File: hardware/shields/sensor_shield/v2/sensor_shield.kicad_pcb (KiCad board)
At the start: 2 copper layers, 34 x 33.8 mm, 4 parts

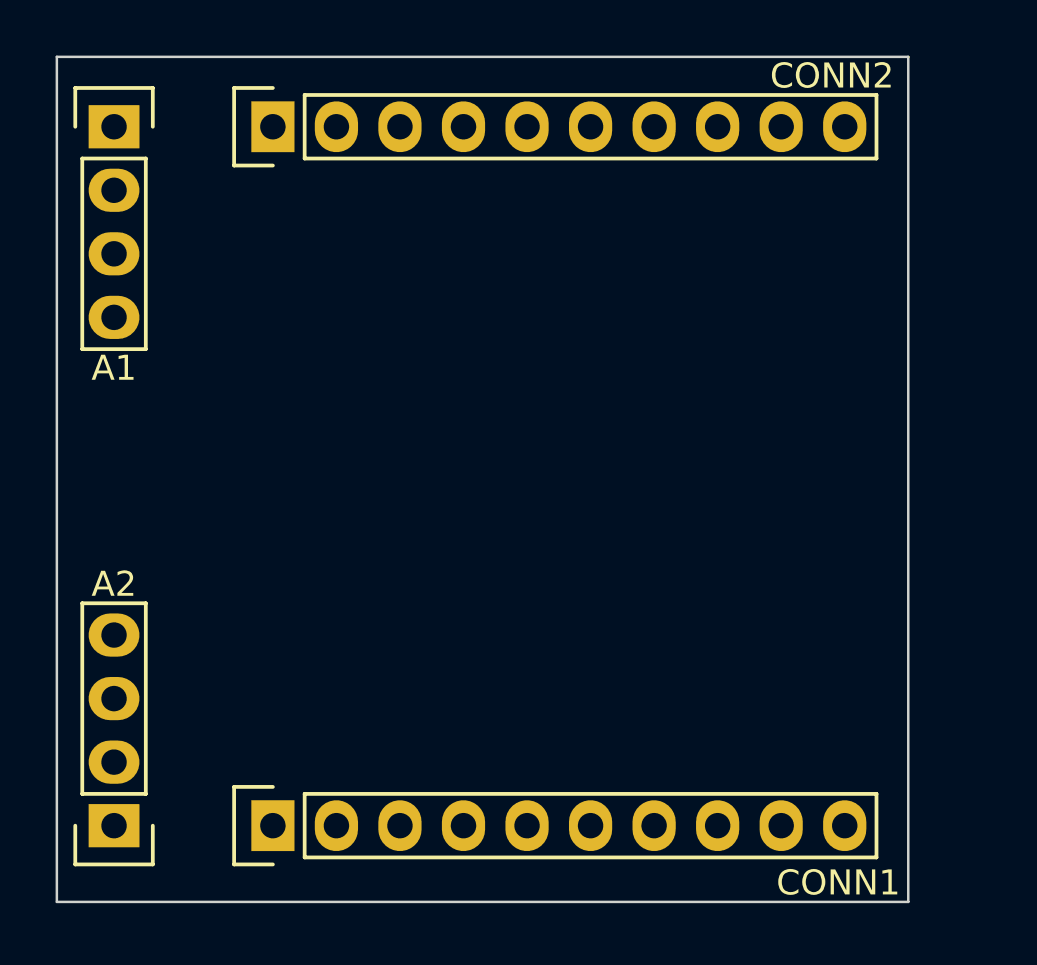
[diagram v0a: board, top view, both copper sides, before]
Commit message: Adding some footprints
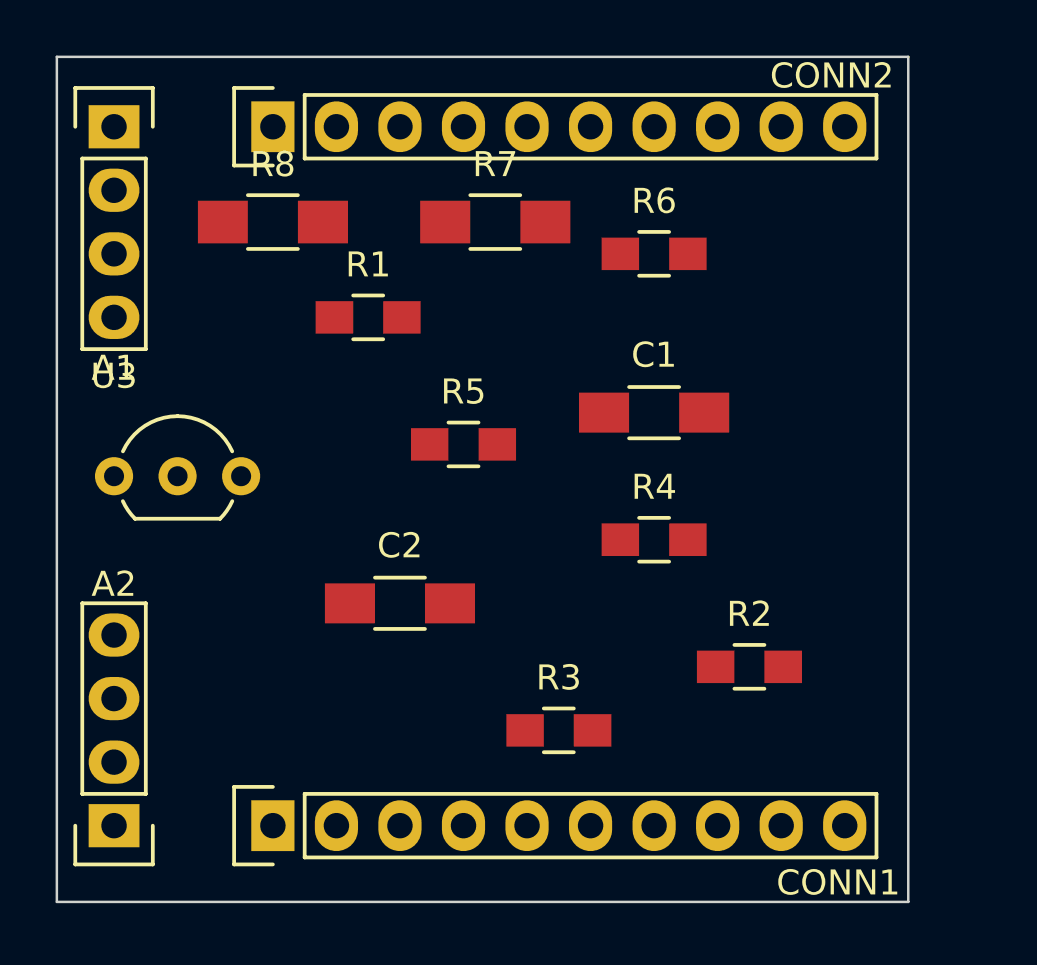
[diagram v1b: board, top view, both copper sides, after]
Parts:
- added C1: 100n, Capacitors_SMD:C_1206_HandSoldering, F.Cu at (62.2, 39.4)
- added C2: 100n, Capacitors_SMD:C_1206_HandSoldering, F.Cu at (52.1, 47.0)
- added R1: 1.8k, Resistors_SMD:R_0805_HandSoldering, F.Cu at (50.8, 35.6)
- added R2: 1.8k, Resistors_SMD:R_0805_HandSoldering, F.Cu at (66.0, 49.5)
- added R3: 100k, Resistors_SMD:R_0805_HandSoldering, F.Cu at (58.4, 52.1)
- added R4: 4.7k, Resistors_SMD:R_0805_HandSoldering, F.Cu at (62.2, 44.5)
- added R5: 200k, Resistors_SMD:R_0805_HandSoldering, F.Cu at (54.6, 40.6)
- added R6: 200k, Resistors_SMD:R_0805_HandSoldering, F.Cu at (62.2, 33.0)
- added R7: 0, Resistors_SMD:R_1206_HandSoldering, F.Cu at (55.9, 31.8)
- added R8: 0, Resistors_SMD:R_1206_HandSoldering, F.Cu at (47.0, 31.8)
- added U3: DS18x20, TO_SOT_Packages_THT:TO-92_Inline_Wide, F.Cu at (40.6, 41.9)

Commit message: Routing of sensor shield complete
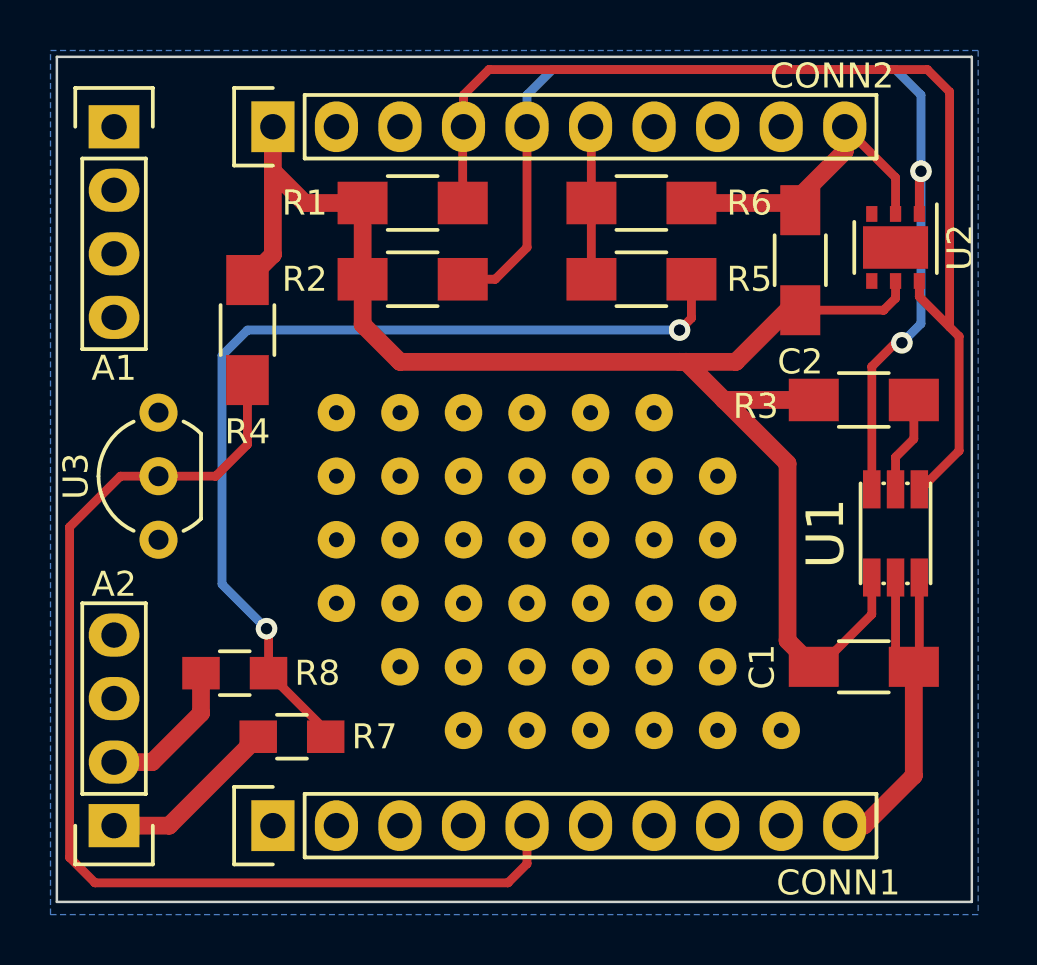
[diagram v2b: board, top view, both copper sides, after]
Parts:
- added ?: , pcb_helpers:pad, F.Cu at (49.5, 39.4)
- added ?: , pcb_helpers:pad, F.Cu at (57.1, 41.9)
- added ?: , pcb_helpers:pad, F.Cu at (59.7, 41.9)
- added ?: , pcb_helpers:pad, F.Cu at (62.2, 41.9)
- added ?: , pcb_helpers:pad, F.Cu at (64.8, 41.9)
- added ?: , pcb_helpers:pad, F.Cu at (49.5, 44.5)
- added ?: , pcb_helpers:pad, F.Cu at (52.1, 44.5)
- added ?: , pcb_helpers:pad, F.Cu at (54.6, 44.5)
- added ?: , pcb_helpers:pad, F.Cu at (57.1, 44.5)
- added ?: , pcb_helpers:pad, F.Cu at (59.7, 44.5)
- added ?: , pcb_helpers:pad, F.Cu at (62.2, 44.5)
- added ?: , pcb_helpers:pad, F.Cu at (52.1, 39.4)
- added ?: , pcb_helpers:pad, F.Cu at (64.8, 44.5)
- added ?: , pcb_helpers:pad, F.Cu at (49.5, 47.0)
- added ?: , pcb_helpers:pad, F.Cu at (52.1, 47.0)
- added ?: , pcb_helpers:pad, F.Cu at (54.6, 47.0)
- added ?: , pcb_helpers:pad, F.Cu at (57.1, 47.0)
- added ?: , pcb_helpers:pad, F.Cu at (59.7, 47.0)
- added ?: , pcb_helpers:pad, F.Cu at (62.2, 47.0)
- added ?: , pcb_helpers:pad, F.Cu at (64.8, 47.0)
- added ?: , pcb_helpers:pad, F.Cu at (52.1, 49.5)
- added ?: , pcb_helpers:pad, F.Cu at (54.6, 49.5)
- added ?: , pcb_helpers:pad, F.Cu at (54.6, 39.4)
- added ?: , pcb_helpers:pad, F.Cu at (57.1, 49.5)
- added ?: , pcb_helpers:pad, F.Cu at (59.7, 49.5)
- added ?: , pcb_helpers:pad, F.Cu at (62.2, 49.5)
- added ?: , pcb_helpers:pad, F.Cu at (64.8, 49.5)
- added ?: , pcb_helpers:pad, F.Cu at (64.8, 52.1)
- added ?: , pcb_helpers:pad, F.Cu at (62.2, 52.1)
- added ?: , pcb_helpers:pad, F.Cu at (59.7, 52.1)
- added ?: , pcb_helpers:pad, F.Cu at (57.1, 52.1)
- added ?: , pcb_helpers:pad, F.Cu at (54.6, 52.1)
- added ?: , pcb_helpers:pad, F.Cu at (67.3, 52.1)
- added ?: , pcb_helpers:pad, F.Cu at (57.1, 39.4)
- added ?: , pcb_helpers:pad, F.Cu at (59.7, 39.4)
- added ?: , pcb_helpers:pad, F.Cu at (62.2, 39.4)
- added ?: , pcb_helpers:pad, F.Cu at (49.5, 41.9)
- added ?: , pcb_helpers:pad, F.Cu at (52.1, 41.9)
- added ?: , pcb_helpers:pad, F.Cu at (54.6, 41.9)
- added U1: TSL2561, BugOne:TMB6, F.Cu at (71.9, 44.2)
- added U2: HTU2XD, Housings_DFN_QFN:DFN-6-1EP_3x3mm_Pitch0.95mm, F.Cu at (71.9, 32.8)
- R1, R2, R3, R4, R5, R6: footprint Resistors_SMD:R_0805_HandSoldering -> Resistors_SMD:R_1206_HandSoldering
- R7, R8: footprint Resistors_SMD:R_1206_HandSoldering -> Resistors_SMD:R_0805_HandSoldering
- moved R7 22.1 mm to (47.8, 52.3)
- moved C2 21.1 mm to (68.1, 33.3), turned to 90 degrees
- moved R2 20.5 mm to (52.6, 34.0)
- moved R4 18.3 mm to (46.0, 36.1), turned to 270 degrees
- moved R8 18.1 mm to (45.5, 49.8)
- moved R3 18.0 mm to (70.6, 38.9)
- moved C1 13.2 mm to (70.6, 49.5)
- moved R5 9.71 mm to (61.7, 34.0), turned to 180 degrees
- moved R1 4.91 mm to (52.6, 31.0)
- moved U3 3.10 mm to (42.4, 44.5), turned to 90 degrees
- moved R6 2.09 mm to (61.7, 31.0)
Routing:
- net VEE: track 0.00 -> 62.0 mm
- net PB1: track 0.00 -> 44.8 mm
- net SDA: track 0.00 -> 44.8 mm, vias 0 -> 2
- net SCL: track 0.00 -> 43.6 mm
- net Net-(R5-Pad1): track 0.00 -> 37.9 mm, vias 0 -> 2
- net GND: track 0.00 -> 27.8 mm
- net VSS: track 0.00 -> 7.23 mm
- net PC3: track 0.00 -> 6.11 mm
- net VCC: track 0.00 -> 5.89 mm
- net Net-(R3-Pad2): track 0.00 -> 3.87 mm
- added copper zone on B.Cu, net GND
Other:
- board size 34 x 33.8 mm -> 36.6 x 33.8 mm
- net class Default: clearance 0.254 -> 0.1524
- net class Power: clearance 0.254 -> 0.1524
- net class Signal: clearance 0.254 -> 0.1524
- rule trace_clearance: 0.254 -> 0.1524
- board text added: "U1"

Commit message: Minor fixes
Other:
- board text removed: "U1"

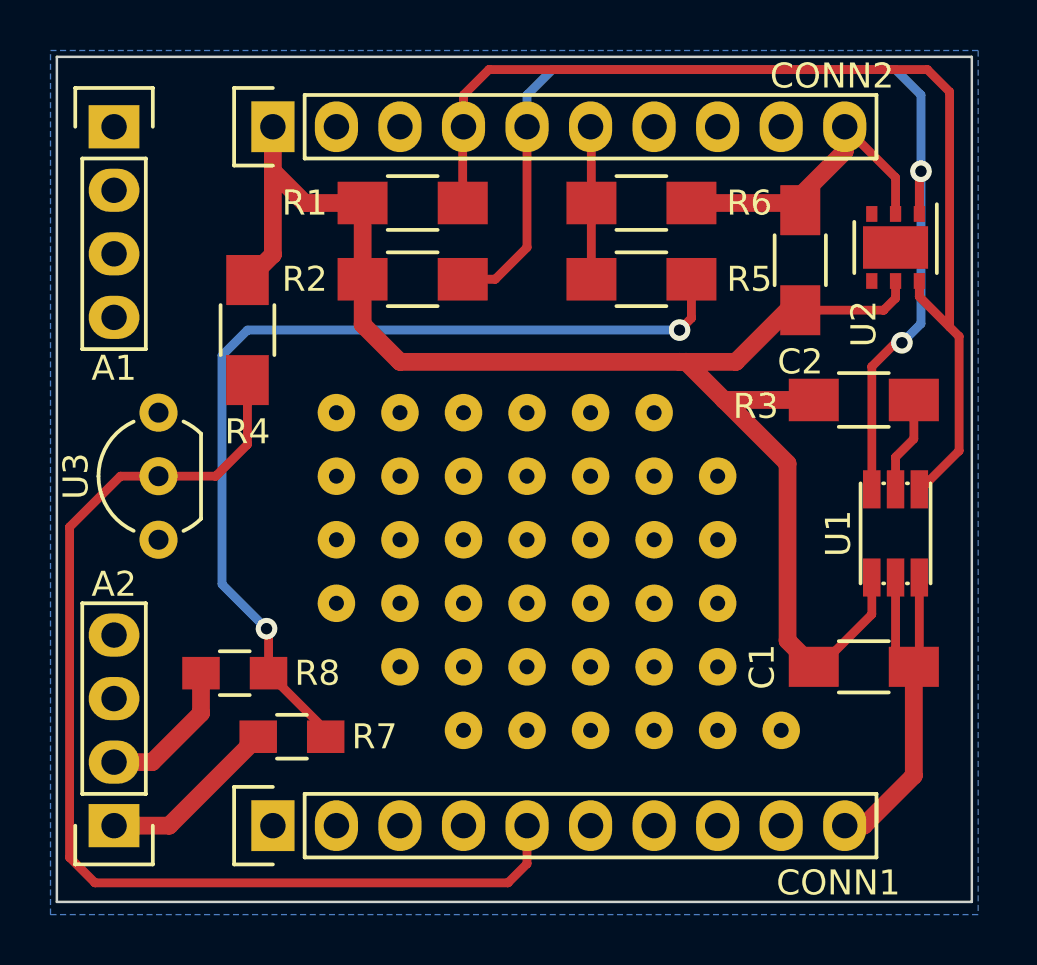
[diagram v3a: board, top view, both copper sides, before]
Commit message: Minor fixes on sensor shield
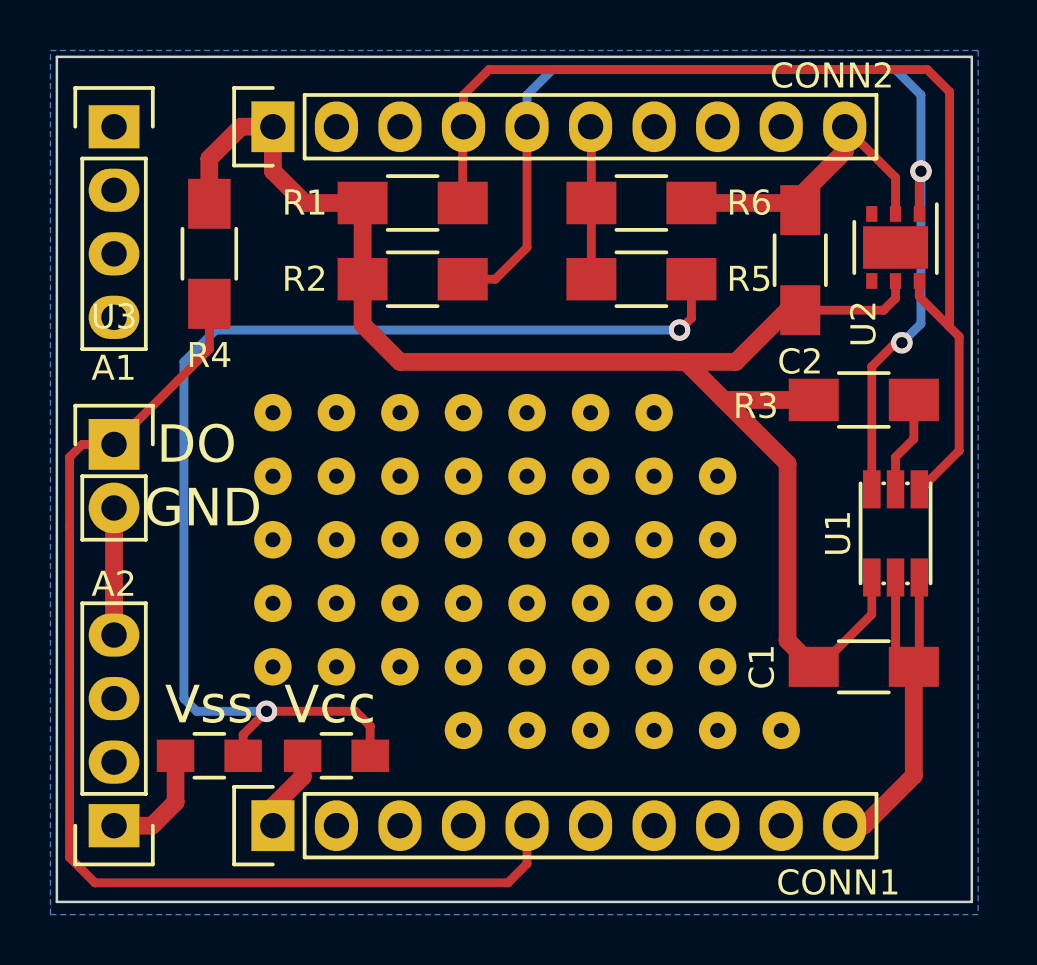
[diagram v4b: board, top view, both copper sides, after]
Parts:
- added ?: , pcb_helpers:pad, F.Cu at (49.5, 49.5)
- added ?: , pcb_helpers:pad, F.Cu at (47.0, 49.5)
- added ?: , pcb_helpers:pad, F.Cu at (47.0, 47.0)
- added ?: , pcb_helpers:pad, F.Cu at (47.0, 44.5)
- added ?: , pcb_helpers:pad, F.Cu at (47.0, 41.9)
- added ?: , pcb_helpers:pad, F.Cu at (47.0, 39.4)
- U3: value DS18x20 -> CONN_01X02; footprint TO_SOT_Packages_THT:TO-92_Inline_Wide -> Pin_Headers:Pin_Header_Straight_1x02
- moved R8 5.24 mm to (49.5, 53.1)
- moved U3 4.20 mm to (40.6, 40.6), turned to 0 degrees
- moved R4 3.41 mm to (44.5, 33.0)
- moved R7 3.39 mm to (44.5, 53.1)
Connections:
- U3 pad 1: GND -> PB1
- U3 pad 2: PB1 -> GND
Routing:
- net Net-(R5-Pad1): track 37.9 -> 47.3 mm
- net GND: track 27.8 -> 32.9 mm
- net VCC: track 5.89 -> 3.29 mm
- net VSS: track 7.23 -> 4.71 mm
- net PB1: track 44.8 -> 45.7 mm
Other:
- board text added: "DO"
- board text added: "GND"
- board text added: "Vcc"
- board text added: "Vss"
